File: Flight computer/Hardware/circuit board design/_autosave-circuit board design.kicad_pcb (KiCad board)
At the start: 4 copper layers, 30.5 x 82.6 mm, 91 parts, among them J1 Conn_01x05, J2 USB_B_Micro, J3 Screw_Terminal_01x04, J4 Conn_01x02, J5 Screw_Terminal_01x04, J6 Conn_Coaxial, J7 Conn_Coaxial, SW1 SW_DPST, U1 IIS2MDC, U10 BMI088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

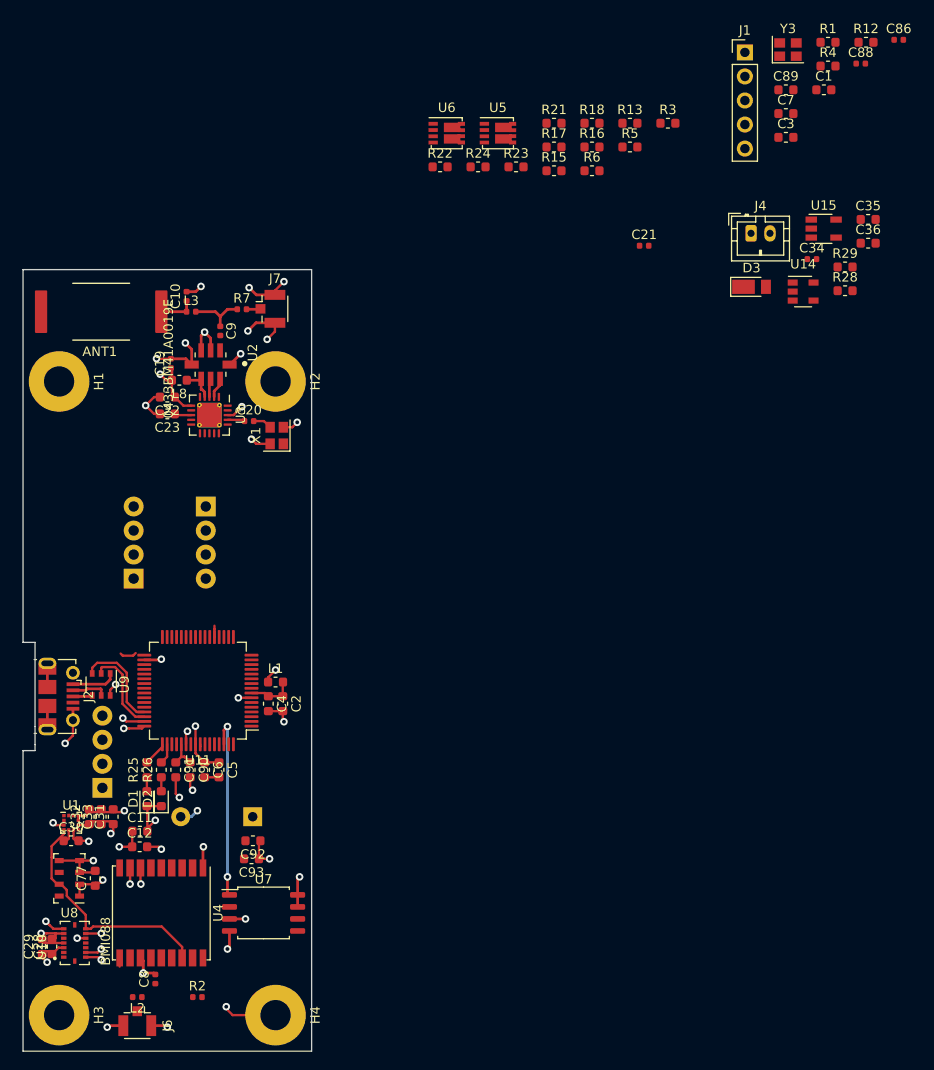
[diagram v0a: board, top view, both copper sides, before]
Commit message: added in the footprint for the 6 terminal block
routed the RF section with the 434 antenna
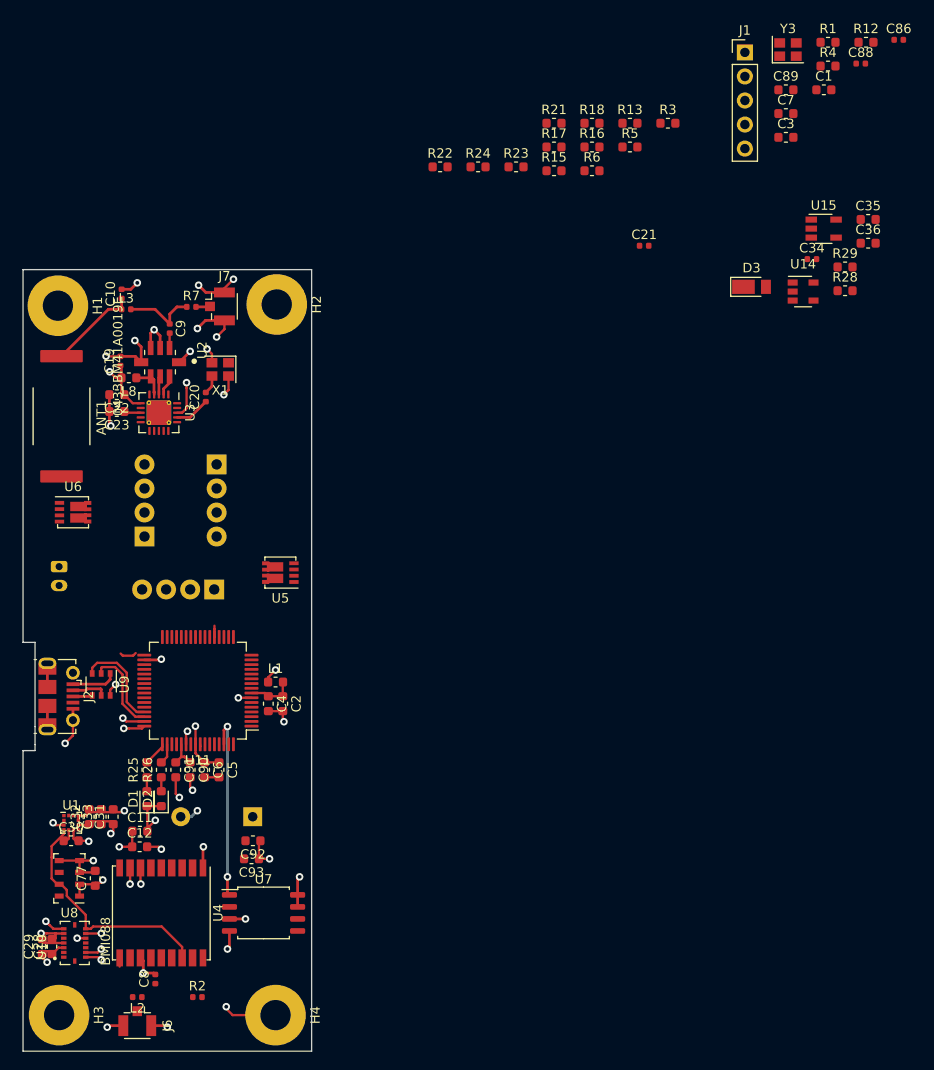
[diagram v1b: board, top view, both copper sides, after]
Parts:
- J4: moved to B.Cu
- moved J4 81.1 mm to (255.3, 277.7), turned to 270 degrees
- moved U6 56.2 mm to (256.7, 272.0)
- moved U5 51.8 mm to (278.6, 278.4), turned to 180 degrees
- moved SW1 24.1 mm to (271.7, 280.2), turned to 180 degrees
- moved ANT1 11.8 mm to (255.5, 261.9), turned to 270 degrees
- moved X1 9.19 mm to (272.3, 256.9), turned to 180 degrees
- moved H2 8.13 mm to (278.3, 250.1)
- moved H1 8.00 mm to (255.1, 250.2)
- moved C10 6.86 mm to (261.9, 248.9)
- moved L3 6.86 mm to (262.4, 250.6)
- moved C19 5.34 mm to (261.7, 256.0)
- moved C23 5.34 mm to (261.4, 261.4)
- moved L8 5.34 mm to (262.6, 257.8)
- moved U2 5.34 mm to (265.9, 256.2)
- moved U3 5.34 mm to (265.8, 261.5)
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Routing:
- net Net-(ANT1-Pad1): track 3.81 -> 9.54 mm
- net Net-(C9-Pad1): track 5.95 -> 7.91 mm
- net Net-(C20-Pad1): track 1.84 -> 3.72 mm
- net GND: track 106.6 -> 108.5 mm
- net Net-(C9-Pad2): track 0.00 -> 1.58 mm
